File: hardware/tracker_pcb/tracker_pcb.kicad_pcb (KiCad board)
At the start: 4 copper layers, 100 x 50 mm, 14 parts, among them IC1 DRV8243HQRXYRQ1, IC2 THVD1426DRLR, IC3 TPS54302DDCR, IC4 DRV8243HQRXYRQ1, J1 2601-1102, J2 2601-1102, J3 2601-1102, U1 ESP32C6_SEEED

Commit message: WIP
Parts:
- removed IC3: TPS54302DDCR, footprint:SOT95P280X110-6N
- removed J2, J3: 2601-1102, footprint:CONN2_2601-1102_WAG
- added C1: 10uF, PCM_JLCPCB:C_1206, F.Cu at (169.5, 91.5)
- added C2: 100nF, PCM_JLCPCB:C_0603, F.Cu at (171.7, 77.3)
- added C3: 33nF, PCM_JLCPCB:C_0603, F.Cu at (171.7, 79.5)
- added C4: 100nF, PCM_JLCPCB:C_0603, F.Cu at (171.7, 81.8)
- added C5: 47pF, PCM_JLCPCB:C_0603, F.Cu at (171.7, 84.0)
- added C6: 10uF, PCM_JLCPCB:C_1206, F.Cu at (150.0, 85.2)
- added D1: SS54, PCM_JLCPCB:D_SMA, F.Cu at (159.0, 92.1)
- added L1: 4.7uH, footprint:IND-SMD_L12.3-W12.3, F.Cu at (162.3, 83.0)
- added R1: 21.5k, PCM_JLCPCB:R_0603, F.Cu at (164.9, 91.0)
- added R2: 52.3k, PCM_JLCPCB:R_0603, F.Cu at (164.9, 93.2)
- added R3: 10k, PCM_JLCPCB:R_0603, F.Cu at (164.9, 95.5)
- added U2: TPS62933FDRLR, footprint:SOTFL50P160X60-8N, F.Cu at (171.5, 87.0)
- added X2: 256-402, footprint:P-256-402, F.Cu at (161.3, 110.5)
- J1: value 2601-1102 -> 256-406; footprint footprint:CONN2_2601-1102_WAG -> footprint:WAGO_256-406
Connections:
- IC1 pad 4: unconnected-(IC1-VM-Pad4) -> /B+

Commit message: wip
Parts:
- removed IC4: DRV8243HQRXYRQ1, footprint:DRV8243HQRXYRQ1
- added U2: DRV8243HQRXYRQ1, footprint:DRV8243HQRXYRQ1, F.Cu at (108.1, 92.6)
- moved U1 53.4 mm to (92.8, 92.6)
- moved U4 16.2 mm to (114.3, 68.6)
- renumbered C3 to C11, C4 to C12, C5 to C13, C6 to C14, C1 to C5, C2 to C6, IC2 to IC1, R2 to R4, R3 to R5, IC1 to U1, U2 to U3, U1 to U4, X2 to X1
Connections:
- J1 pad 1_1: unconnected-(J1-1-Pad1_1) -> /M1_2
- J1 pad 1_2: unconnected-(J1-1__1-Pad1_2) -> /M1_2
- J1 pad 2_1: unconnected-(J1-2-Pad2_1) -> GND
- J1 pad 2_2: unconnected-(J1-2__1-Pad2_2) -> GND
- J1 pad 3_1: unconnected-(J1-3-Pad3_1) -> /M1_1
- J1 pad 3_2: unconnected-(J1-3__1-Pad3_2) -> /M1_1
- J1 pad 4_1: unconnected-(J1-4-Pad4_1) -> /M2_2
- J1 pad 4_2: unconnected-(J1-4__1-Pad4_2) -> /M2_2
- J1 pad 5_1: unconnected-(J1-5-Pad5_1) -> GND
- J1 pad 5_2: unconnected-(J1-5__1-Pad5_2) -> GND
- J1 pad 6_1: unconnected-(J1-6-Pad6_1) -> /M2_1
- J1 pad 6_2: unconnected-(J1-6__1-Pad6_2) -> /M2_1
- U1 pad 14: unconnected-(IC1-MODE-Pad14) -> Net-(JP1-B)
- U1 pad 2: unconnected-(IC1-IPROPI-Pad2) -> GND
- U1 pad 3: unconnected-(IC1-NSLEEP-Pad3) -> /nSLEEP
- U1 pad 5: unconnected-(IC1-OUT2-Pad5) -> /M1_2
- U1 pad 6: unconnected-(IC1-GND-Pad6) -> GND
- U1 pad 7: unconnected-(IC1-OUT1-Pad7) -> /M1_1
- U1 pad 8: unconnected-(IC1-DRVOFF-Pad8) -> GND

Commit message: Adding 8244 models
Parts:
- added C1: 100nF, PCM_JLCPCB:C_0603, F.Cu at (122.7, 83.5)
- added C10: 100nF, PCM_JLCPCB:C_0603, F.Cu at (122.7, 94.7)
- added C2: 100nF, PCM_JLCPCB:C_0603, F.Cu at (122.7, 85.7)
- added C7: 100nF, PCM_JLCPCB:C_0603, F.Cu at (122.7, 88.0)
- added C8: 100nF, PCM_JLCPCB:C_0603, F.Cu at (122.7, 90.2)
- added C9: 100nF, PCM_JLCPCB:C_0603, F.Cu at (122.7, 92.5)
- added IC2: DRV8244HQRYJRQ1, footprint:DRV8244HQRYJRQ1, F.Cu at (127.9, 87.1)
- added R2: 21.5k, PCM_JLCPCB:R_0603, F.Cu at (126.4, 93.0)
- added R3: 21.5k, PCM_JLCPCB:R_0603, F.Cu at (126.4, 95.2)

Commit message: wip
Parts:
- removed U1: DRV8243HQRXYRQ1, footprint:DRV8243HQRXYRQ1
- L1: footprint footprint:IND-SMD_L12.3-W12.3 -> Inductor_SMD:L_10.4x10.4_H4.8
- moved C6 94.7 mm to (80.5, 103.0), turned to -90 degrees
- moved U3 92.8 mm to (79.5, 99.0)
- moved C5 92.2 mm to (78.0, 103.0), turned to -90 degrees
- moved R1 88.0 mm to (77.2, 99.0), turned to 90 degrees
- moved L1 78.5 mm to (84.0, 87.5), turned to 90 degrees
- moved D1 76.3 mm to (83.5, 103.0), turned to -90 degrees
- moved R4 75.6 mm to (89.3, 94.0)
- moved R5 75.6 mm to (89.3, 96.3)
- moved C11 75.6 mm to (96.1, 80.4)
- moved C12 75.6 mm to (96.1, 82.6)
- moved C13 75.6 mm to (96.1, 84.9)
- moved X1 69.4 mm to (92.0, 107.8), turned to -90 degrees
- moved RJ1 27.7 mm to (142.8, 136.3)
- moved RJ2 27.3 mm to (120.9, 135.5)
- moved J1 13.5 mm to (114.5, 107.8)
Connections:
- IC2 pad 10: unconnected-(IC2-DRVOFF-Pad10) -> GND
- IC2 pad 16: unconnected-(IC2-MODE-Pad16) -> Net-(IC2-MODE)
- IC2 pad 2: unconnected-(IC2-IPROPI-Pad2) -> GND
- IC2 pad 3: unconnected-(IC2-NSLEEP-Pad3) -> /nSLEEP
- IC2 pad 4: unconnected-(IC2-VM-Pad4) -> /B+
- IC2 pad 5: unconnected-(IC2-OUT2_1-Pad5) -> /M1_2
- IC2 pad 6: unconnected-(IC2-OUT2_2-Pad6) -> /M1_2
- IC2 pad 7: unconnected-(IC2-GND-Pad7) -> GND
- IC2 pad 8: unconnected-(IC2-OUT1_1-Pad8) -> /M1_1
- IC2 pad 9: unconnected-(IC2-OUT1_2-Pad9) -> /M1_1

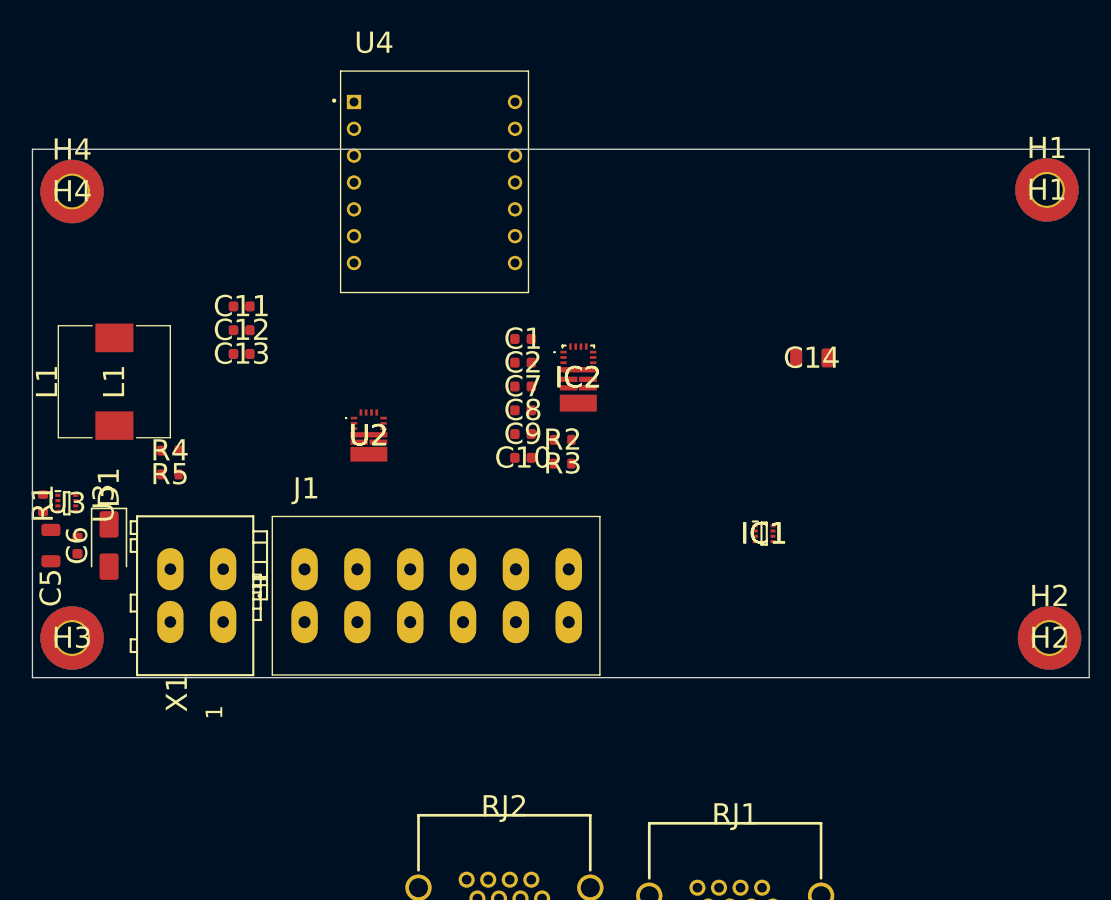
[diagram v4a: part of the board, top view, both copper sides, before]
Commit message: Adding motor caps
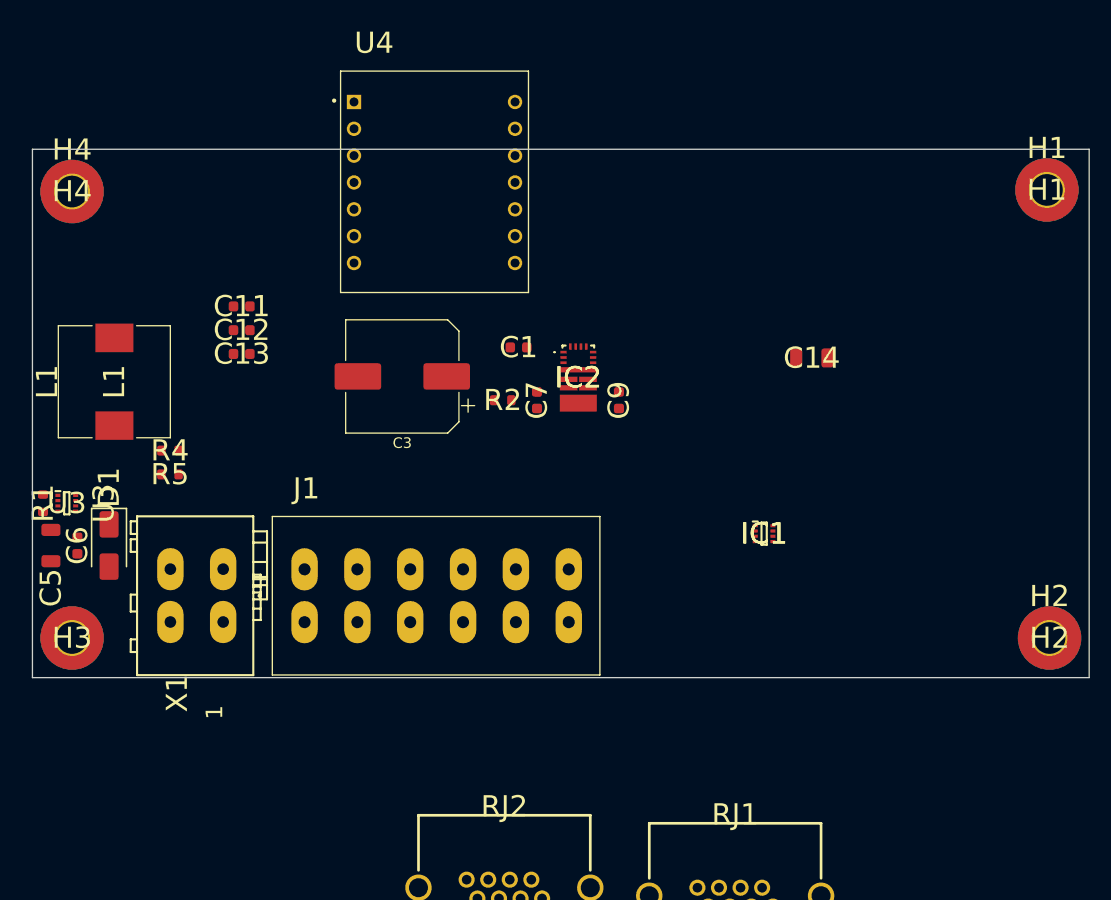
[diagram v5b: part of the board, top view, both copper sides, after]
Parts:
- removed C10, C2, C8: 100nF, PCM_JLCPCB:C_0603
- removed R3: 21.5k, PCM_JLCPCB:R_0603
- removed U2: DRV8243HQRXYRQ1, footprint:DRV8243HQRXYRQ1
- added C3: 470uF, Capacitor_SMD:CP_Elec_10x12.5, F.Cu at (111.2, 87.0)
- moved C9 9.62 mm to (131.8, 89.2), turned to -90 degrees
- moved R2 6.81 mm to (120.8, 89.2)
- moved C7 1.85 mm to (124.0, 89.2), turned to -90 degrees
- moved C1 0.91 mm to (122.2, 84.2)

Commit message: Routing begins
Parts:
- added C1: 100nF, Capacitor_SMD:C_0603_1608Metric, F.Cu at (178.7, 88.8)
- added C3: 470uF, Capacitor_SMD:CP_Elec_10x12.5, F.Cu at (177.5, 81.5)
- added C7: 100nF, Capacitor_SMD:C_0603_1608Metric, F.Cu at (178.7, 91.3)
- added C9: 100nF, Capacitor_SMD:C_0603_1608Metric, F.Cu at (178.7, 93.8)
- added IC1: DRV8244HQRYJRQ1, footprint:DRV8244HQRYJRQ1, F.Cu at (173.4, 92.3)
- added JP1: SolderJumper_2_Open, Resistor_SMD:R_0402_1005Metric_Pad0.72x0.64mm_HandSolder, F.Cu at (182.3, 88.5)
- added JP2: SolderJumper_2_Open, Resistor_SMD:R_0402_1005Metric_Pad0.72x0.64mm_HandSolder, F.Cu at (109.5, 90.5)
- added R2: 21.5k, Resistor_SMD:R_0603_1608Metric, F.Cu at (178.7, 96.3)
- C10: renamed from C9; footprint PCM_JLCPCB:C_0603 -> Capacitor_SMD:C_0603_1608Metric
- C11, C12, C13, C6: footprint PCM_JLCPCB:C_0603 -> Capacitor_SMD:C_0603_1608Metric
- C14: footprint PCM_JLCPCB:C_1206 -> Capacitor_SMD:C_0603_1608Metric
- C2: renamed from C1; footprint PCM_JLCPCB:C_0603 -> Capacitor_SMD:C_0603_1608Metric
- C5: footprint PCM_JLCPCB:C_1206 -> Capacitor_SMD:C_1206_3216Metric
- C8: renamed from C7; footprint PCM_JLCPCB:C_0603 -> Capacitor_SMD:C_0603_1608Metric
- D1: footprint PCM_JLCPCB:D_SMA -> Diode_SMD:D_SMA
- L1: footprint Inductor_SMD:L_10.4x10.4_H4.8 -> Inductor_SMD:L_12x12mm_H6mm
- R1, R4, R5: footprint PCM_JLCPCB:R_0603 -> Resistor_SMD:R_0603_1608Metric
- R3: renamed from R2; footprint PCM_JLCPCB:R_0603 -> Resistor_SMD:R_0603_1608Metric
- moved C14 48.3 mm to (101.8, 82.5)
- moved RJ2 40.9 mm to (149.2, 106.0)
- moved RJ1 39.9 mm to (168.7, 106.0)
- moved U2 36.5 mm to (147.5, 83.7)
- moved C8 21.4 mm to (105.0, 99.0), turned to 180 degrees
- moved R1 20.8 mm to (78.8, 78.2), turned to -90 degrees
- moved C6 19.7 mm to (81.0, 83.3)
- moved C5 18.5 mm to (77.5, 84.5)
- moved IC2 18.3 mm to (111.6, 95.4)
- moved R5 17.8 mm to (89.0, 78.5), turned to 90 degrees
- moved U1 17.7 mm to (83.5, 81.8)
- moved C10 16.7 mm to (118.2, 99.0), turned to 0 degrees
- moved H1 13.8 mm to (186.0, 69.0)
- moved R4 13.4 mm to (95.2, 82.0), turned to 180 degrees
- moved H2 12.5 mm to (185.0, 112.0)
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- renumbered C3 to C4, IC1 to IC3, U3 to U1, U4 to U2
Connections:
- net /B+ renamed /VIN
- net Net-(C13-Pad1) renamed /VDD
- IC2 pad 11: unconnected-(IC2-EN/IN1-Pad11) -> /PWM1_F
- IC2 pad 12: unconnected-(IC2-PH/IN2-Pad12) -> /PWM1_R
- U2 pad 1: unconnected-(U4-D0-Pad1) -> /PWM1_F
- U2 pad 2: unconnected-(U4-D1-Pad2) -> /PWM1_R
- U2 pad 3: unconnected-(U4-D2-Pad3) -> /PWM2_F
- U2 pad 4: unconnected-(U4-D3-Pad4) -> /PWM2_R
- U2 pad 5: unconnected-(U4-D4-Pad5) -> /nSLEEP
- X1 pad L1.1: Net-(D1-Pad2) -> unconnected-(X1-PadL1.1)
- X1 pad L1.2: Net-(D1-Pad2) -> GND
- X1 pad L2.1: GND -> unconnected-(X1-PadL2.1)
- X1 pad L2.2: GND -> Net-(D1-Pad2)
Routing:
- net /M1_2: vias 0 -> 14
- added copper zone on B.Cu, net /M1_2
- added copper zone on F.Cu, net /M1_2
- added copper zone on F.Cu, net GND
- added copper zone on In1.Cu, net GND
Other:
- board size 100 x 50 mm -> 114.3 x 50 mm

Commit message: More layout
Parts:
- H1, H2, H3, H4: footprint MountingHole:MountingHole_3mm_Pad_TopBottom -> MountingHole:MountingHole_3.5mm_Pad_Via
- moved C2 21.4 mm to (133.0, 80.2)
- moved JP2 21.4 mm to (128.5, 80.7)
- moved R3 21.4 mm to (128.5, 78.7)
- moved C4 11.6 mm to (111.5, 83.9)
- moved H2 2.86 mm to (187.3, 113.8)
- moved H3 2.02 mm to (80.2, 113.8)
- moved H1 1.28 mm to (187.3, 68.7)
- moved H4 0.80 mm to (80.2, 68.7)
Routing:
- net /nSLEEP: track 0.00 -> 4.44 mm
- net /PWM1_F: track 0.00 -> 3.98 mm
- net /PWM1_R: track 0.00 -> 3.14 mm
- net GND: track 0.00 -> 3.01 mm, vias 0 -> 1
- added copper zone on B.Cu, net /M1_1
- added copper zone on F.Cu, net /M1_1
- added copper zone on F.Cu, net /VIN
- added copper zone on In2.Cu, net /VIN
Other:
- board size 114.3 x 50 mm -> 119 x 57 mm

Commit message: Hierarcical sheets
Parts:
- removed C11: 33nF, Capacitor_SMD:C_0603_1608Metric
- removed C12, C7, C9: 100nF, Capacitor_SMD:C_0603_1608Metric
- removed C13: 47pF, Capacitor_SMD:C_0603_1608Metric
- removed C14: 10uF, Capacitor_SMD:C_0603_1608Metric
- removed D1: SS54, Diode_SMD:D_SMA
- removed L1: 4.7uH, Inductor_SMD:L_12x12mm_H6mm
- removed R2: 21.5k, Resistor_SMD:R_0603_1608Metric
- removed R4: 52.3k, Resistor_SMD:R_0603_1608Metric
- removed R5: 10k, Resistor_SMD:R_0603_1608Metric
- removed U1: TPS62933FDRLR, footprint:SOTFL50P160X60-8N
- added C15: 10uF, Capacitor_SMD:C_1206_3216Metric, F.Cu at (103.2, 71.8)
- added C16: 100nF, Capacitor_SMD:C_0603_1608Metric, F.Cu at (102.8, 74.2)
- added C17: 33nF, Capacitor_SMD:C_0603_1608Metric, F.Cu at (84.5, 93.6)
- added C18: 100nF, Capacitor_SMD:C_0603_1608Metric, F.Cu at (84.5, 92.1)
- added C19: 47pF, Capacitor_SMD:C_0603_1608Metric, F.Cu at (83.5, 96.1)
- added C20: 10uF, Capacitor_SMD:C_0603_1608Metric, F.Cu at (89.0, 75.0)
- added D2: SS54, Diode_SMD:D_SMA, F.Cu at (94.8, 96.3)
- added L2: 4.7uH, Inductor_SMD:L_12x12mm_H6mm, F.Cu at (84.5, 83.1)
- added R6: 21.5k, Resistor_SMD:R_0603_1608Metric, F.Cu at (88.6, 96.0)
- added R7: 52.3k, Resistor_SMD:R_0603_1608Metric, F.Cu at (85.2, 96.1)
- added R8: 10k, Resistor_SMD:R_0603_1608Metric, F.Cu at (86.9, 96.1)
- added U3: TPS62933FDRLR, footprint:SOTFL50P160X60-8N, F.Cu at (87.7, 92.6)
- C5: value 10uF -> 100nF; footprint Capacitor_SMD:C_1206_3216Metric -> Capacitor_SMD:C_0603_1608Metric
- moved IC1 116.4 mm to (57.0, 93.5)
- moved C3 116.0 mm to (61.6, 82.3)
- moved JP1 116.0 mm to (66.4, 89.3)
- moved C1 116.0 mm to (62.7, 89.6)
- moved R3 84.4 mm to (46.2, 97.1)
- moved C2 28.5 mm to (107.0, 91.8), turned to 180 degrees
- moved JP2 25.6 mm to (102.9, 79.2)
- moved R1 24.7 mm to (62.7, 97.1), turned to 0 degrees
- moved C6 21.5 mm to (62.7, 94.6), turned to 0 degrees
- moved C5 16.6 mm to (62.7, 92.1), turned to 0 degrees
- moved C10 3.83 mm to (114.4, 99.1), turned to 180 degrees
- moved C8 3.50 mm to (108.5, 99.1), turned to 0 degrees
- moved C4 2.60 mm to (111.4, 81.3)
- moved IC2 2.48 mm to (111.5, 92.9)
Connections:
- C1 pad 1: /VIN -> /Motor Control DRV8244_1/VM
- C10 pad 1: /M1_1 -> /Motor Control DRV8244_1/OUT1
- C2 pad 1: /VIN -> /Motor Control DRV8244_1/VM
- C3 pad 1: /VIN -> /Motor Control DRV8244_1/VM
- C4 pad 1: /VIN -> /Motor Control DRV8244_1/VM
- C5 pad 1: /VIN -> /Motor Control DRV8244_2/OUT2
- C6 pad 1: /VIN -> /Motor Control DRV8244_2/OUT1
- C8 pad 1: /M1_2 -> /Motor Control DRV8244_1/OUT2
- IC1 pad 11: /PWM2_F -> /Motor Control DRV8244_2/PWMF
- IC1 pad 12: /PWM2_R -> /Motor Control DRV8244_2/PWMR
- IC1 pad 3: /nSLEEP -> /Motor Control DRV8244_1/nSLEEP
- IC1 pad 4: /VIN -> /Motor Control DRV8244_1/VM
- IC1 pad 5: /M2_2 -> /Motor Control DRV8244_2/OUT2
- IC1 pad 6: /M2_2 -> /Motor Control DRV8244_2/OUT2
- IC1 pad 8: /M2_1 -> /Motor Control DRV8244_2/OUT1
- IC1 pad 9: /M2_1 -> /Motor Control DRV8244_2/OUT1
- IC2 pad 11: /PWM1_F -> /Motor Control DRV8244_1/PWMF
- IC2 pad 12: /PWM1_R -> /Motor Control DRV8244_1/PWMR
- IC2 pad 3: /nSLEEP -> /Motor Control DRV8244_1/nSLEEP
- IC2 pad 4: /VIN -> /Motor Control DRV8244_1/VM
- IC2 pad 5: /M1_2 -> /Motor Control DRV8244_1/OUT2
- IC2 pad 6: /M1_2 -> /Motor Control DRV8244_1/OUT2
- IC2 pad 8: /M1_1 -> /Motor Control DRV8244_1/OUT1
- IC2 pad 9: /M1_1 -> /Motor Control DRV8244_1/OUT1
- J1 pad 1_1: /M1_2 -> /Motor Control DRV8244_1/OUT1
- J1 pad 1_2: /M1_2 -> /Motor Control DRV8244_1/OUT1
- J1 pad 3_1: /M1_1 -> /Motor Control DRV8244_1/OUT2
- J1 pad 3_2: /M1_1 -> /Motor Control DRV8244_1/OUT2
- J1 pad 4_1: /M2_2 -> /Motor Control DRV8244_2/OUT1
- J1 pad 4_2: /M2_2 -> /Motor Control DRV8244_2/OUT1
- J1 pad 6_1: /M2_1 -> /Motor Control DRV8244_2/OUT2
- J1 pad 6_2: /M2_1 -> /Motor Control DRV8244_2/OUT2
- R1 pad 2: Net-(U1-RT) -> Net-(JP1-A)
- U2 pad 1: /PWM1_F -> /Motor Control DRV8244_1/nSLEEP
- U2 pad 2: /PWM1_R -> /Motor Control DRV8244_1/PWMF
- U2 pad 3: /PWM2_F -> /Motor Control DRV8244_1/PWMR
- U2 pad 4: /PWM2_R -> /Motor Control DRV8244_2/PWMF
- U2 pad 5: /nSLEEP -> /Motor Control DRV8244_2/PWMR
- X1 pad L1.1: unconnected-(X1-PadL1.1) -> /Power/VRAW
- X1 pad L1.2: GND -> /Power/VRAW
- X1 pad L2.1: unconnected-(X1-PadL2.1) -> GND
- X1 pad L2.2: Net-(D1-Pad2) -> GND
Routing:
- net /Motor Control DRV8244_1/OUT1: track 0.00 -> 6.15 mm
- net Net-(U3-FB): track 0.00 -> 5.04 mm
- net /nSLEEP: track 4.44 -> 0.00 mm
- net Net-(U3-SW): track 0.00 -> 4.37 mm
- net /PWM1_F: track 3.98 -> 0.00 mm
- net /Motor Control DRV8244_1/PWMF: track 0.00 -> 3.98 mm
- net /PWM1_R: track 3.14 -> 0.00 mm
- net Net-(U3-SS): track 0.00 -> 1.95 mm
- net Net-(U3-RT): track 0.00 -> 1.90 mm
- net GND: track 3.01 -> 1.11 mm, vias 1 -> 2
- net Net-(U3-BST): track 0.00 -> 1.74 mm
- net /M1_2: vias 14 -> 0
- added copper zone on B.Cu, net /Motor Control DRV8244_1/OUT1
- added copper zone on F.Cu, net /Motor Control DRV8244_1/OUT1
- added copper zone on B.Cu, net /Motor Control DRV8244_1/OUT2
- added copper zone on F.Cu, net /Motor Control DRV8244_1/OUT2
- added copper zone on F.Cu, net /Motor Control DRV8244_1/VM
- added copper zone on In2.Cu, net /Motor Control DRV8244_1/VM
- added copper zone on F.Cu, net /Power/VRAW
- added copper zone on F.Cu, net Net-(U3-FB)
- added copper zone on F.Cu, net Net-(U3-SW)
- removed copper zone on B.Cu, net /M1_1
- removed copper zone on F.Cu, net /M1_1
- removed copper zone on B.Cu, net /M1_2
- removed copper zone on F.Cu, net /M1_2
- removed copper zone on F.Cu, net /VIN
- removed copper zone on In2.Cu, net /VIN
